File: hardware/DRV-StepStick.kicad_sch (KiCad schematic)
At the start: 23 parts, among them J1 PCIe_Stepper, J2 Conn_01x04_Male, J3 StepStickL, J4 StepStickR, J5 Conn_01x04, J6 Conn_02x04_Odd_Even, J7 Conn_01x02, J8 Screw_Terminal_01x02, U1 24LC02, U2 74LVC1G06

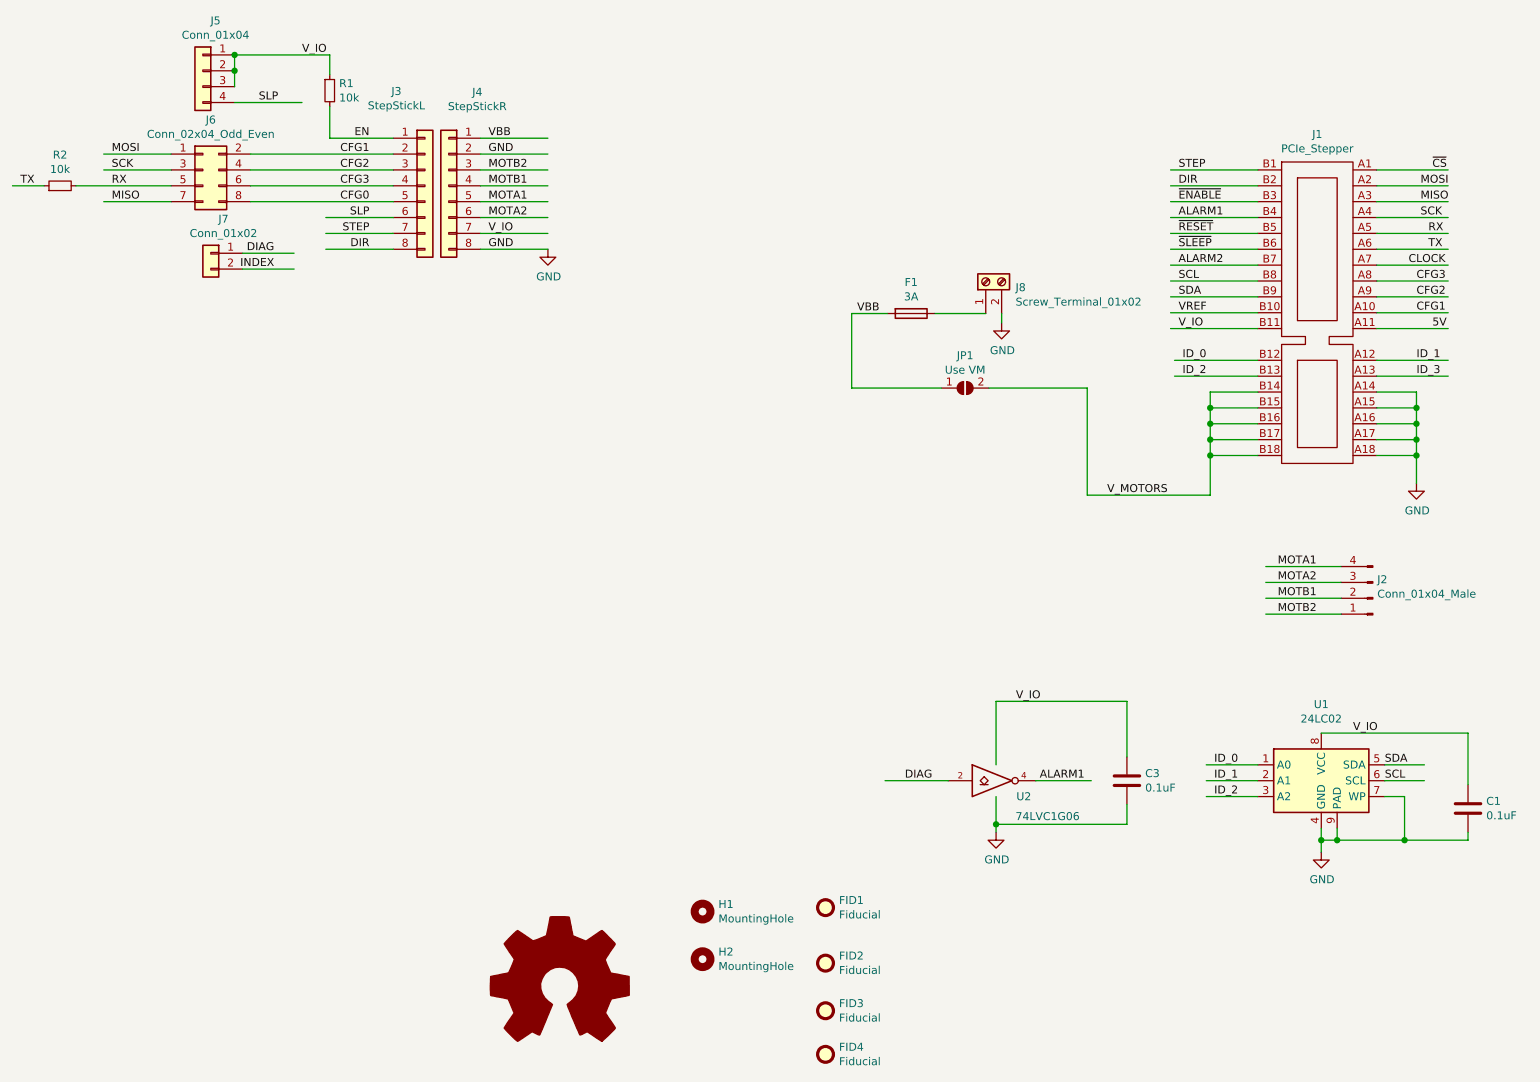
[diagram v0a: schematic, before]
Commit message: Update the StepStick driver schematics, revert the routing.
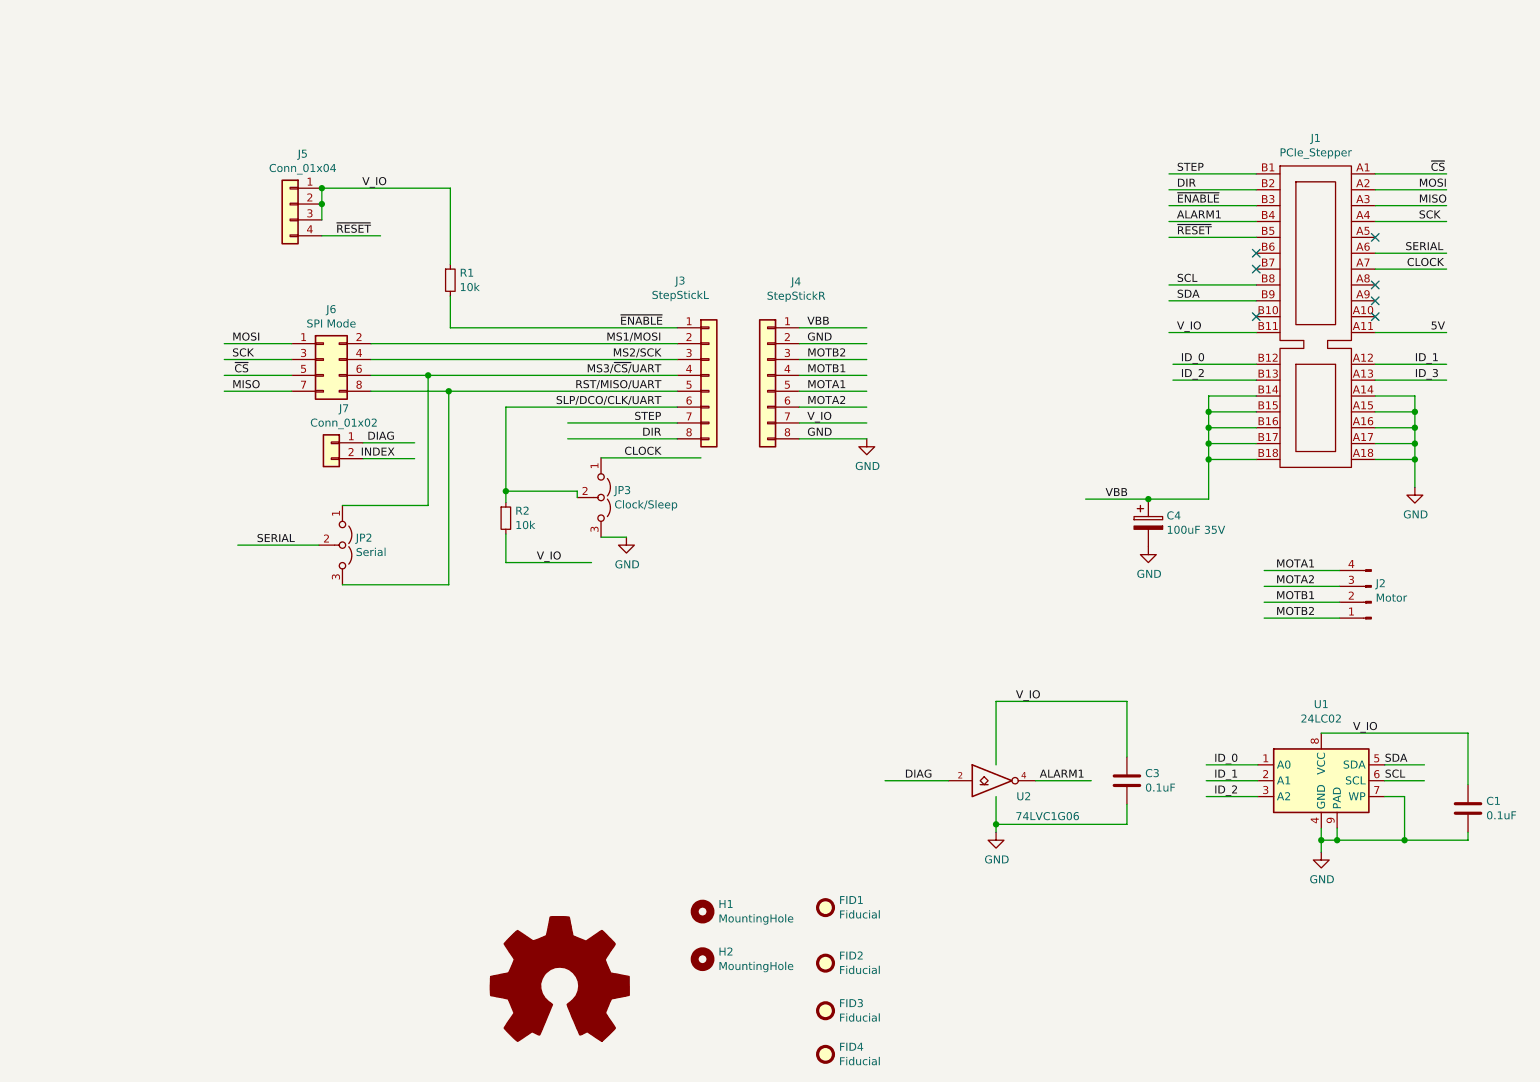
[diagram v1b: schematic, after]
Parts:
- removed F1: 3A, Fuse:Fuse_1206_3216Metric, symbol Device:Fuse
- removed J8: Screw_Terminal_01x02, TerminalBlock_Phoenix:TerminalBlock_Phoenix_PT-1,5-2-3.5-H_1x02_P3.50mm_Horizontal, symbol Connector:Screw_Terminal_01x02
- removed JP1: Use VM, Jumper:SolderJumper-2_P1.3mm_Open_TrianglePad1.0x1.5mm, symbol Jumper:SolderJumper_2_Open
- added C4: 100uF 35V, Capacitor_SMD:CP_Elec_6.3x7.7, symbol Device:CP
- added JP2: Serial, Connector_PinHeader_2.54mm:PinHeader_1x03_P2.54mm_Vertical, symbol Jumper:Jumper_3_Open
- added JP3: Clock/Sleep, Connector_PinHeader_2.54mm:PinHeader_1x03_P2.54mm_Vertical, symbol Jumper:Jumper_3_Open
- J2: value Conn_01x04_Male -> Motor
- J6: value Conn_02x04_Odd_Even -> SPI Mode
- R1, R2: LCSC Part # (none) -> C29718; Part # (none) -> 4D03WGJ0103T5E
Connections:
- net EN is gone; now on net ~ENABLE: J3.1 (Pin_1), R1.2
- net V_MOTORS is gone; now on net VBB: J1.B14, J1.B15, J1.B16, J1.B17, J1.B18
- net CLOCK: now also JP3.1 (A)
- net GND: now also C4.2, JP3.3 (B)
- net VBB: now also C4.1
- net VCC: now also R2.2
- net ~CS: now also J6.5 (Pin_5)
- net ~RESET: now also J5.4 (Pin_4)
- net ALARM2: no longer names the net of J1.B7
- net CFG0 renamed RST/MISO/UART
- net RST/MISO/UART: now also JP2.3 (B)
- net CFG1 renamed MS1/MOSI
- net MS1/MOSI: no longer J1.A10
- net CFG2 renamed MS2/SCK
- net MS2/SCK: no longer J1.A9
- net CFG3 renamed MS3/~CS/UART
- net MS3/~CS/UART: now also JP2.1 (A); no longer J1.A8
- removed net RX: J1.A5, J6.5 (Pin_5), R2.2
- net SLP renamed SLP/DCO/CLK/UART
- net SLP/DCO/CLK/UART: now also R2.1, JP3.2 (C); no longer J5.4 (Pin_4)
- net TX renamed SERIAL
- net SERIAL: now also JP2.2 (C); no longer R2.1
- net VREF: no longer names the net of J1.B10
- net ~SLEEP: no longer names the net of J1.B6
- no-connect marks 0 -> 7
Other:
- moved on the sheet: J1, J2, J3, J4, J5, J6, J7, R1

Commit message: Routed the StepStick adapter board 2 layers.
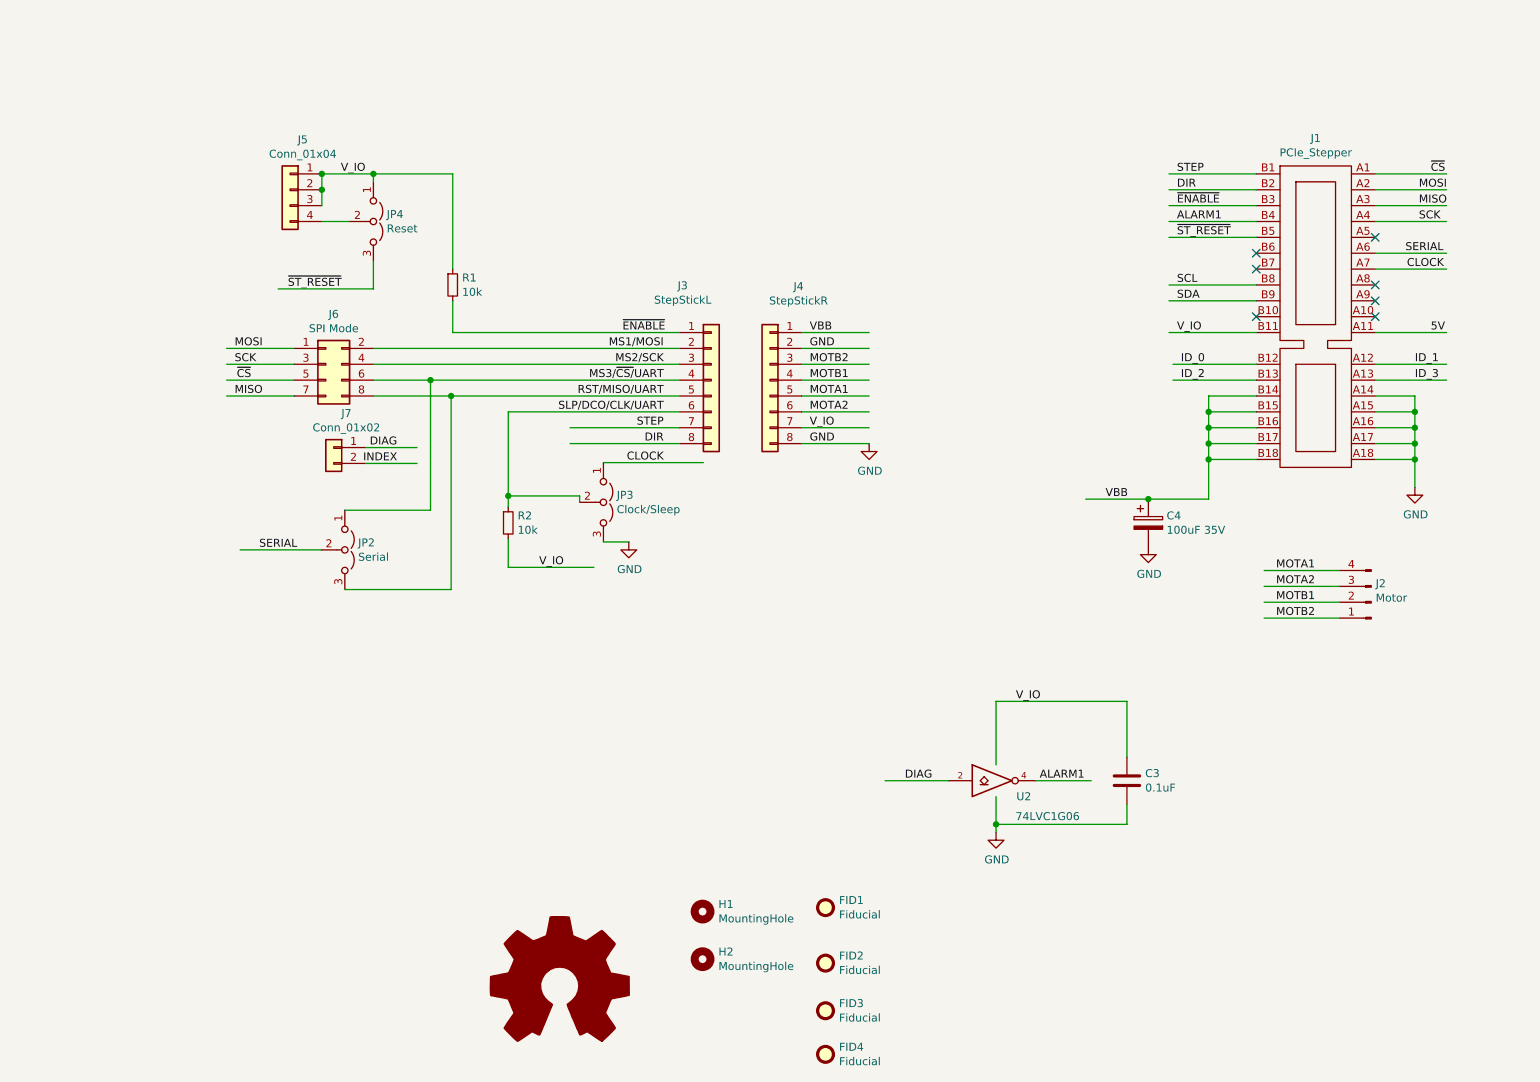
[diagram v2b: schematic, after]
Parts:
- removed C1: 0.1uF, PrntrBoardV2:C_0603_1608Metric, symbol Device:C
- removed U1: 24LC02, PrntrBoardV2:TDFN-8-1EP_3x2mm_P0.5mm_EP1.56x1.45mm, symbol 24lc02:24LC02
- added JP4: Reset, Connector_PinHeader_2.54mm:PinHeader_1x03_P2.54mm_Vertical, symbol Jumper:Jumper_3_Open
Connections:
- net VCC: now also JP4.1 (A)
- net ~RESET: no longer names the net of J5.4 (Pin_4)
- net ~RESET: now also JP4.2 (C); no longer J1.B5
- new net ~ST_RESET: J1.B5, JP4.3 (B)
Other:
- moved on the sheet: J3, J4, J5, J6, J7, JP2, JP3, R1, R2

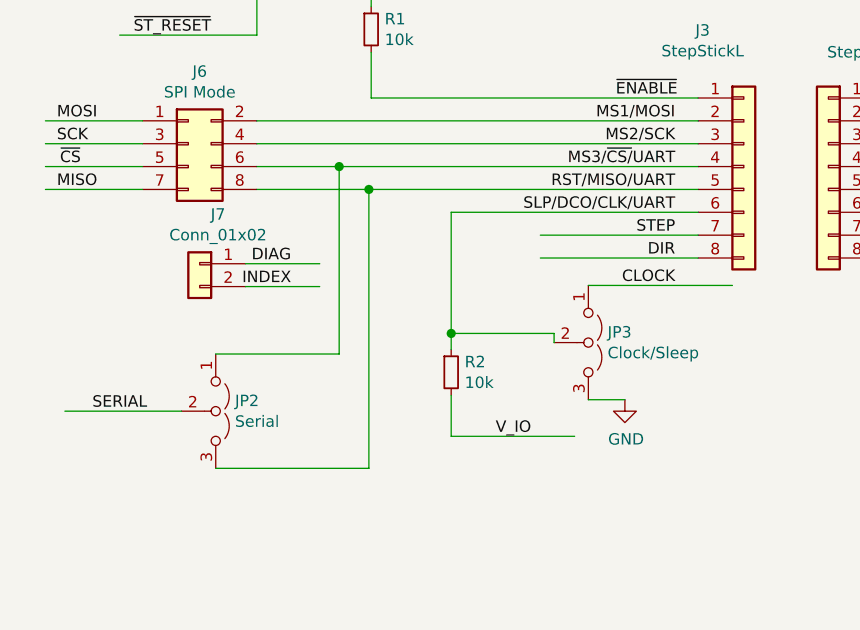
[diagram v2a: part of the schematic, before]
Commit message: Move the configuration jumpers out of the way.
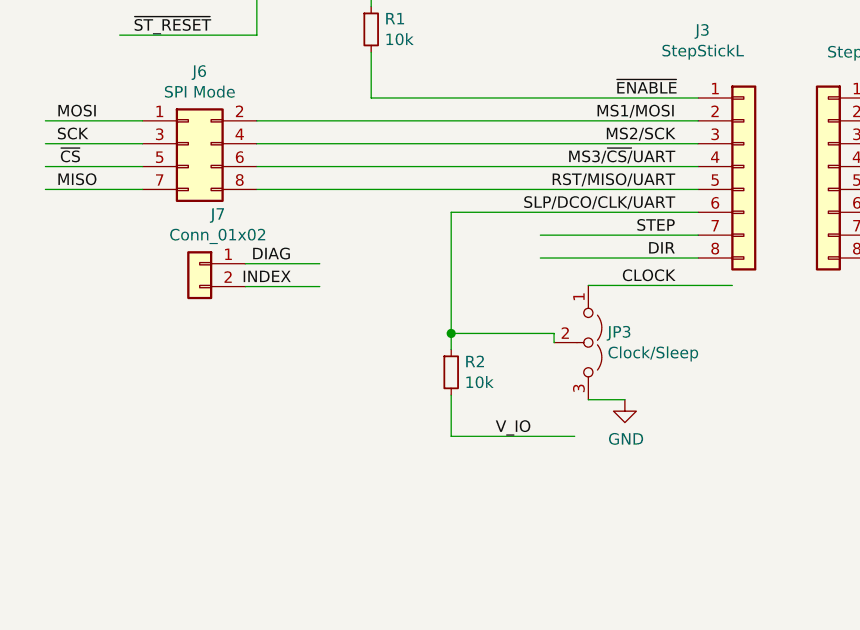
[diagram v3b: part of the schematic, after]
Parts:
- removed JP2: Serial, Connector_PinHeader_2.54mm:PinHeader_1x03_P2.54mm_Vertical, symbol Jumper:Jumper_3_Open
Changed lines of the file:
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@@
   (junction (at 80.01 52.07) (diameter 1.016) (color 0 0 0 0))
   (junction (at 88.265 49.53) (diameter 1.016) (color 0 0 0 0))
-  (junction (at 97.409 82.55) (diameter 1.016) (color 0 0 0 0))
-  (junction (at 100.711 85.09) (diameter 1.016) (color 0 0 0 0))
   (junction (at 109.855 101.092) (diameter 1.016) (color 0 0 0 0))
   (junction (at 187.96 153.67) (diameter 1.016) (color 0 0 0 0))
@@
     (stroke (width 0) (type solid) (color 0 0 0 0))
   )
-  (wire (pts (xy 66.929 109.728) (xy 79.883 109.728))
-    (stroke (width 0) (type solid) (color 0 0 0 0))
-  )
   (wire (pts (xy 73.025 67.945) (xy 88.265 67.945))
     (stroke (width 0) (type solid) (color 0 0 0 0))
@@
     (stroke (width 0) (type solid) (color 0 0 0 0))
   )
-  (wire (pts (xy 83.693 103.378) (xy 97.409 103.378))
-    (stroke (width 0) (type solid) (color 0 0 0 0))
-  )
-  (wire (pts (xy 83.693 116.078) (xy 100.711 116.078))
-    (stroke (width 0) (type solid) (color 0 0 0 0))
-  )
   (wire (pts (xy 86.995 93.345) (xy 95.25 93.345))
     (stroke (width 0) (type solid) (color 0 0 0 0))
@@
     (stroke (width 0) (type solid) (color 0 0 0 0))
   )
-  (wire (pts (xy 88.265 82.55) (xy 97.409 82.55))
-    (stroke (width 0) (type solid) (color 0 0 0 0))
-  )
-  (wire (pts (xy 88.265 85.09) (xy 100.711 85.09))
-    (stroke (width 0) (type solid) (color 0 0 0 0))
-  )
-  (wire (pts (xy 97.409 82.55) (xy 97.409 103.378))
-    (stroke (width 0) (type solid) (color 0 0 0 0))
-  )
-  (wire (pts (xy 97.409 82.55) (xy 137.287 82.55))
-    (stroke (width 0) (type solid) (color 0 0 0 0))
-  )
-  (wire (pts (xy 100.711 85.09) (xy 137.287 85.09))
-    (stroke (width 0) (type solid) (color 0 0 0 0))
-  )
-  (wire (pts (xy 100.711 116.078) (xy 100.711 85.09))
+  (wire (pts (xy 88.265 82.55) (xy 137.287 82.55))
+    (stroke (width 0) (type solid) (color 0 0 0 0))
+  )
+  (wire (pts (xy 88.265 85.09) (xy 137.287 85.09))
     (stroke (width 0) (type solid) (color 0 0 0 0))
   )
@@
   )
   (label "~CS" (at 68.707 82.55 180)
-    (effects (font (size 1.27 1.27)) (justify right bottom))
-  )
-  (label "SERIAL" (at 76.073 109.728 180)
     (effects (font (size 1.27 1.27)) (justify right bottom))
   )
@@
     )
   )
-  (symbol (lib_id "Jumper:Jumper_3_Open") (at 83.693 109.728 270) (unit 1)
-    (in_bom yes) (on_board yes)
-    (property "Reference" "JP2" (id 0) (at 85.827 108.579 90)
-      (effects (font (size 1.27 1.27)) (justify left))
-    )
-    (property "Value" "Serial" (id 1) (at 85.827 110.877 90)
-      (effects (font (size 1.27 1.27)) (justify left))
-    )
-    (property "Footprint" "Connector_PinHeader_2.54mm:PinHeader_1x03_P2.54mm_Vertical" (id 2) (at 83.693 109.728 0)
-      (effects (font (size 1.27 1.27)) hide)
-    )
-    (property "Datasheet" "~" (id 3) (at 83.693 109.728 0)
-      (effects (font (size 1.27 1.27)) hide)
-    )
-  )
   (symbol (lib_id "Jumper:Jumper_3_Open") (at 88.265 57.15 270) (unit 1)
     (in_bom yes) (on_board yes)
@@
       (reference "J7") (unit 1) (value "Conn_01x02") (footprint "Connector_PinSocket_2.54mm:PinSocket_1x02_P2.54mm_Vertical")
     )
-    (path "/7f03273a-923a-45b4-93fe-00d716d067d5"
-      (reference "JP2") (unit 1) (value "Serial") (footprint "Connector_PinHeader_2.54mm:PinHeader_1x03_P2.54mm_Vertical")
-    )
     (path "/57182310-957a-4d8f-a6a6-d0824195d12a"
